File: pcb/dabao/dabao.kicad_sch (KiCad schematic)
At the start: 68 parts, among them J1 Conn_01x05, J2 USB_C_Receptacle_USB2.0_16P, J3 Conn_01x04, J4 MagConn_01x04_Pin, J5 Conn_Battery, J6 Conn_01x04, J7 Conn_01x04, J8 Display, SW1 SW_RESET, SW2 SW_POWER, U1 nice_nano, U2 MCP23017_SP

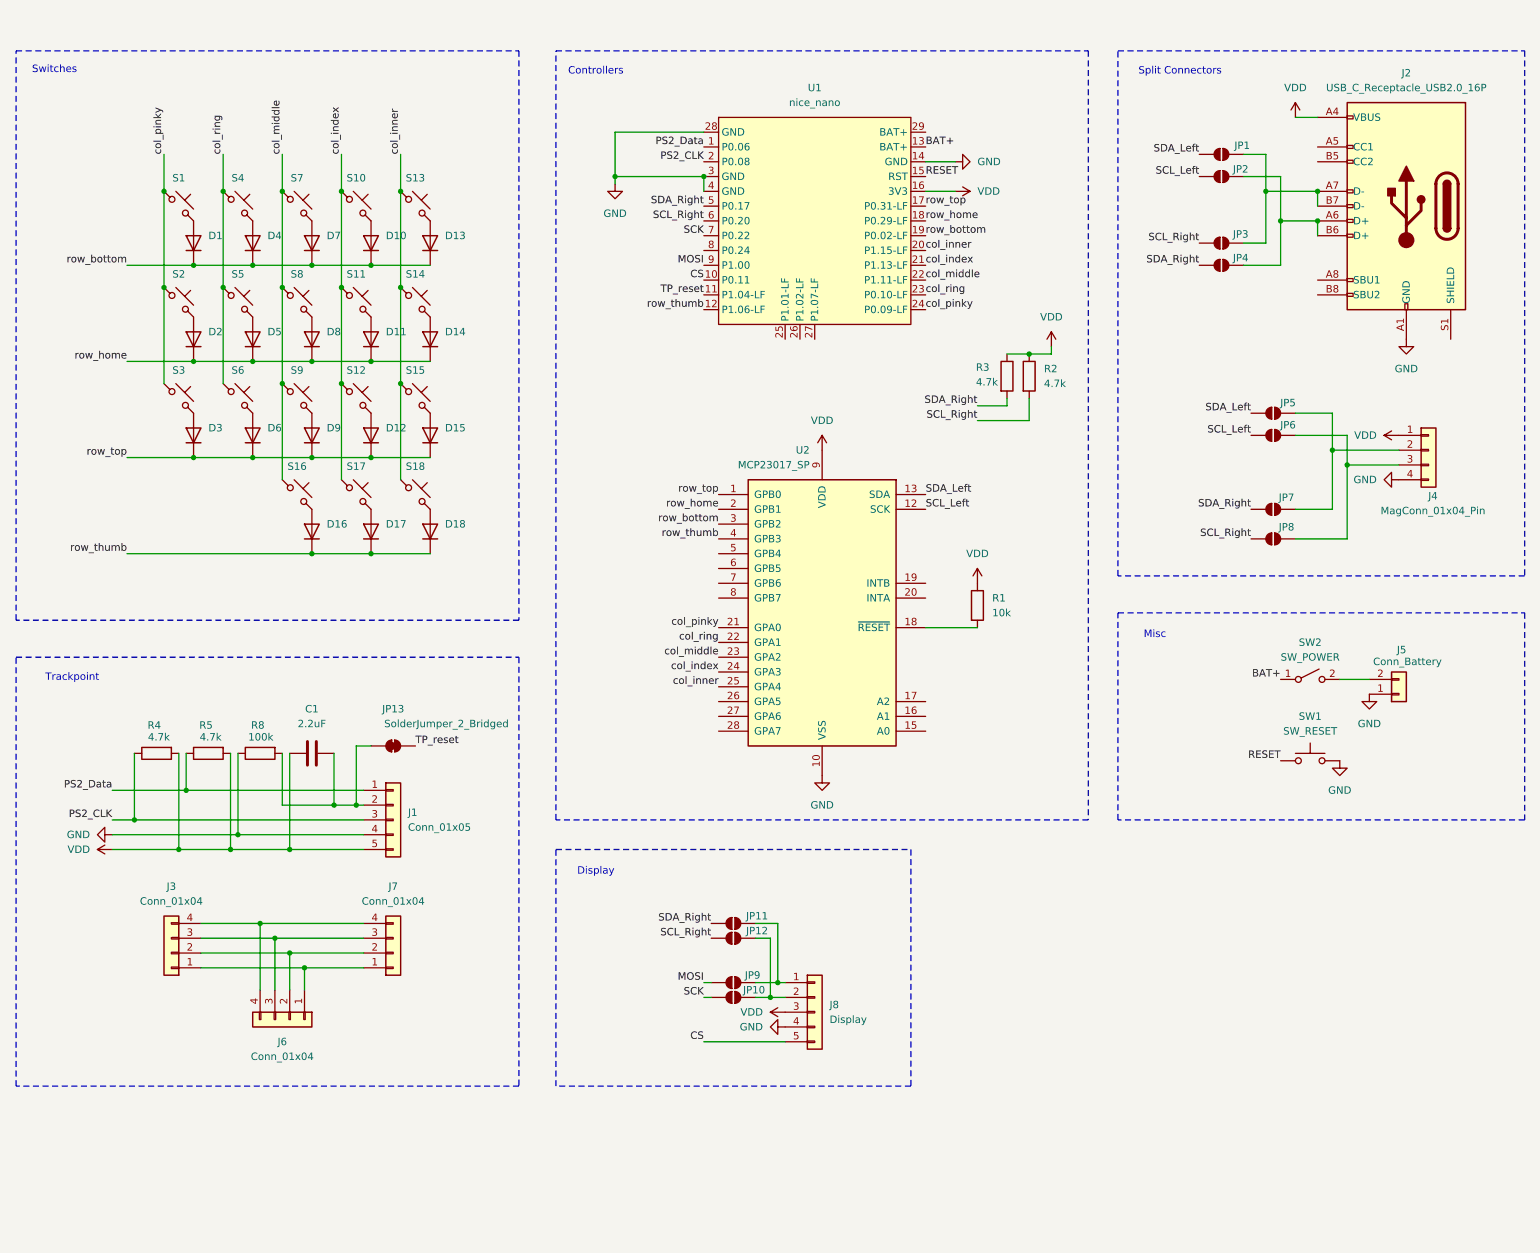
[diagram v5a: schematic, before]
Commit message: Move trackpoint to thumb, routing
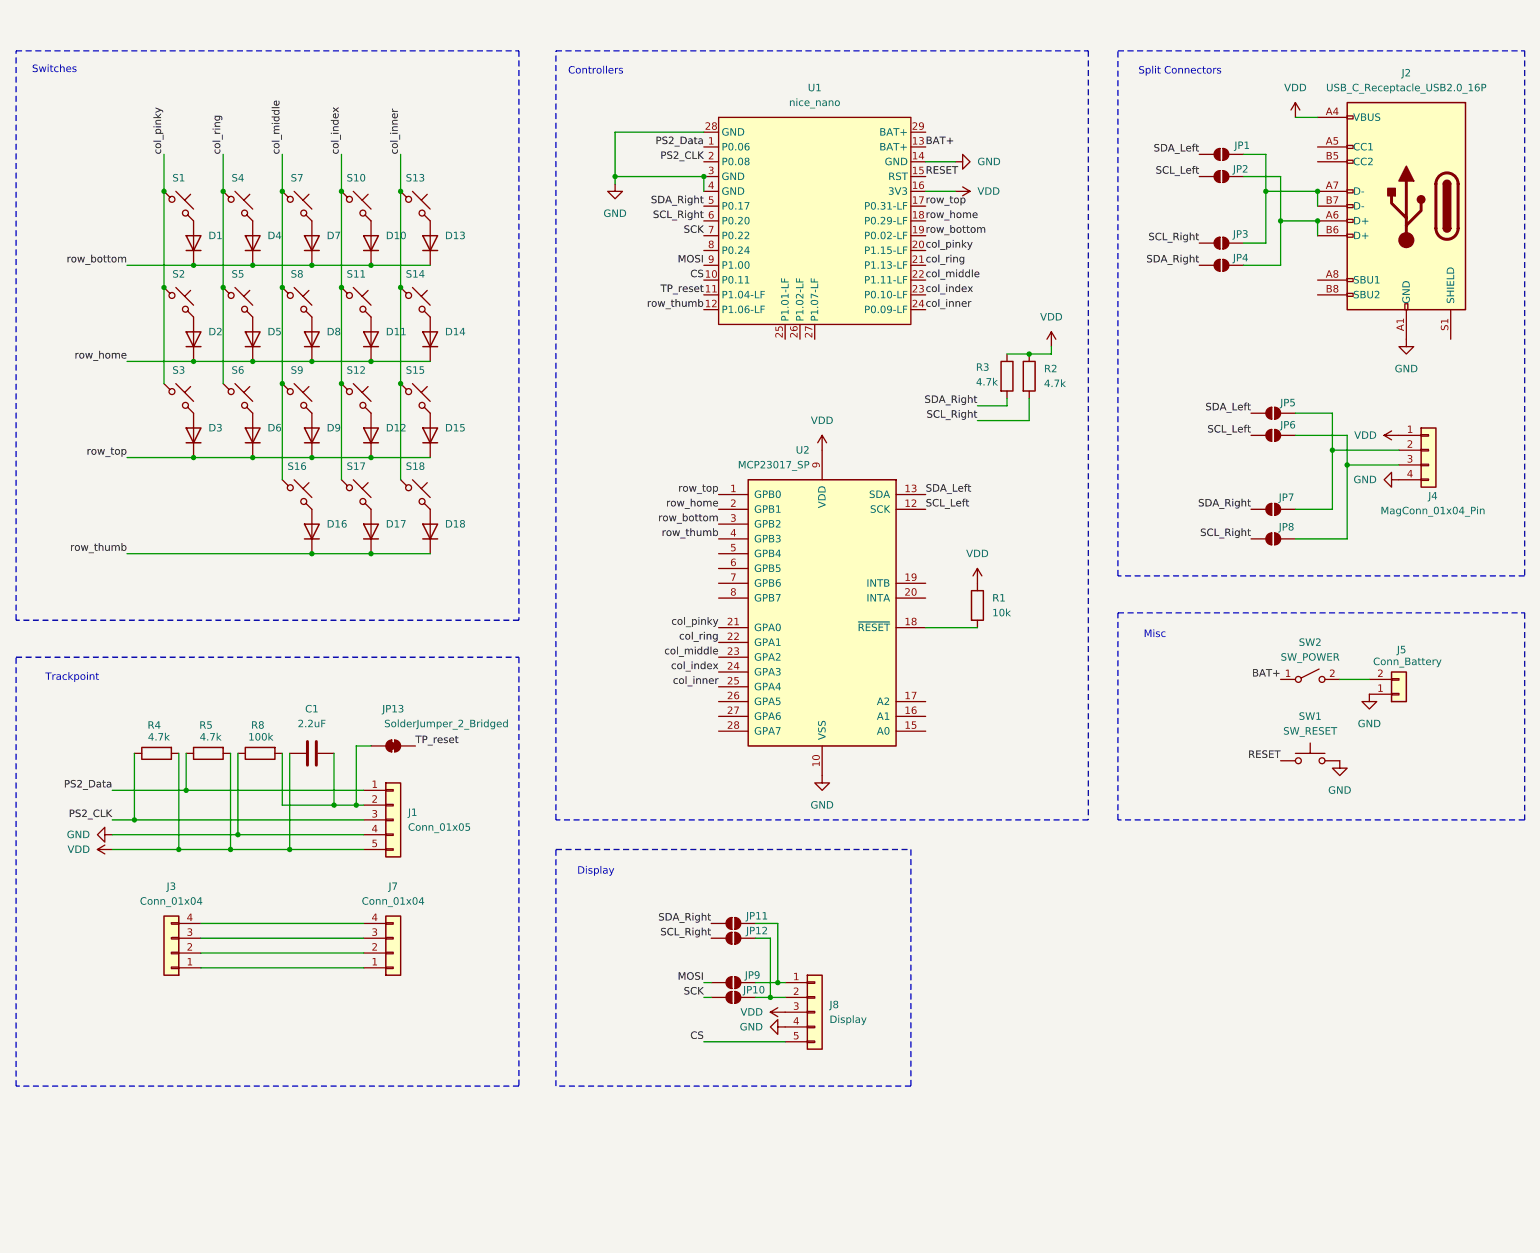
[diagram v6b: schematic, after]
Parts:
- removed J6: Conn_01x04, Library:TPSensorModule_Connector, symbol Connector_Generic:Conn_01x04
- S14, S16: footprint Library:SW_PG1350_reversible -> Library:Kailh_socket_PG1350_optional_reversible.kicad_mod
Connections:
- net col_index: now also U1.23 (P0.10-LF); no longer U1.21 (P1.13-LF)
- net col_inner: now also U1.24 (P0.09-LF); no longer U1.20 (P1.15-LF)
- net col_pinky: now also U1.20 (P1.15-LF); no longer U1.24 (P0.09-LF)
- net col_ring: now also U1.21 (P1.13-LF); no longer U1.23 (P0.10-LF)
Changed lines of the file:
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@@
 	)
 	(junction
-		(at 68.58 172.72)
-		(diameter 0)
-		(color 0 0 0 0)
-	)
-	(junction
 		(at 73.66 144.78)
 		(diameter 0)
@@
 	)
 	(junction
-		(at 63.5 167.64)
-		(diameter 0)
-		(color 0 0 0 0)
-	)
-	(junction
-		(at 66.04 170.18)
-		(diameter 0)
-		(color 0 0 0 0)
-	)
-	(junction
 		(at 242.57 39.37)
 		(diameter 0)
@@
 	)
 	(junction
-		(at 60.96 165.1)
-		(diameter 0)
-		(color 0 0 0 0)
-	)
-	(junction
 		(at 44.45 55.88)
 		(diameter 0)
@@
 	(wire
 		(pts
-			(xy 68.58 172.72) (xy 78.74 172.72)
+			(xy 50.8 172.72) (xy 78.74 172.72)
 		)
 		(stroke
@@
 	(wire
 		(pts
-			(xy 50.8 165.1) (xy 60.96 165.1)
+			(xy 50.8 165.1) (xy 78.74 165.1)
 		)
 		(stroke
@@
 	(wire
 		(pts
-			(xy 68.58 172.72) (xy 68.58 176.53)
-		)
-		(stroke
-			(width 0)
-			(type default)
-		)
-	)
-	(wire
-		(pts
 			(xy 80.01 52.07) (xy 90.17 52.07)
 		)
@@
 	(wire
 		(pts
-			(xy 50.8 170.18) (xy 66.04 170.18)
-		)
-		(stroke
-			(width 0)
-			(type default)
-		)
-	)
-	(wire
-		(pts
 			(xy 242.57 44.45) (xy 242.57 46.99)
 		)
@@
 	(wire
 		(pts
-			(xy 50.8 167.64) (xy 63.5 167.64)
-		)
-		(stroke
-			(width 0)
-			(type default)
-		)
-	)
-	(wire
-		(pts
 			(xy 245.11 83.82) (xy 256.54 83.82)
 		)
@@
 	(wire
 		(pts
-			(xy 50.8 172.72) (xy 68.58 172.72)
-		)
-		(stroke
-			(width 0)
-			(type default)
-		)
-	)
-	(wire
-		(pts
 			(xy 64.77 55.88) (xy 64.77 72.39)
 		)
@@
 	(wire
 		(pts
-			(xy 63.5 167.64) (xy 78.74 167.64)
+			(xy 50.8 167.64) (xy 78.74 167.64)
 		)
 		(stroke
@@
 	(wire
 		(pts
-			(xy 66.04 170.18) (xy 78.74 170.18)
+			(xy 50.8 170.18) (xy 78.74 170.18)
 		)
 		(stroke
@@
 	(wire
 		(pts
-			(xy 66.04 170.18) (xy 66.04 176.53)
-		)
-		(stroke
-			(width 0)
-			(type default)
-		)
-	)
-	(wire
-		(pts
 			(xy 38.1 52.07) (xy 49.53 52.07)
 		)
@@
 	(wire
 		(pts
-			(xy 60.96 165.1) (xy 60.96 176.53)
-		)
-		(stroke
-			(width 0)
-			(type default)
-		)
-	)
-	(wire
-		(pts
 			(xy 229.87 52.07) (xy 236.22 52.07)
 		)
@@
 	(wire
 		(pts
-			(xy 60.96 165.1) (xy 78.74 165.1)
-		)
-		(stroke
-			(width 0)
-			(type default)
-		)
-	)
-	(wire
-		(pts
 			(xy 44.45 39.37) (xy 44.45 55.88)
 		)
@@
 	(wire
 		(pts
-			(xy 63.5 167.64) (xy 63.5 176.53)
-		)
-		(stroke
-			(width 0)
-			(type default)
-		)
-	)
-	(wire
-		(pts
 			(xy 184.15 76.2) (xy 189.23 76.2)
 		)
@@
 		)
 	)
+	(label "col_inner"
+		(at 175.26 59.69 0)
+		(effects
+			(font
+				(size 1.27 1.27)
+			)
+			(justify left bottom)
+		)
+	)
 	(label "col_pinky"
 		(at 139.7 114.3 180)
@@
 		)
 	)
+	(label "col_ring"
+		(at 175.26 52.07 0)
+		(effects
+			(font
+				(size 1.27 1.27)
+			)
+			(justify left bottom)
+		)
+	)
 	(label "SDA_Right"
 		(at 138.43 165.1 180)
@@
 		)
 	)
-	(label "col_middle"
-		(at 175.26 54.61 0)
-		(effects
-			(font
-				(size 1.27 1.27)
-			)
-			(justify left bottom)
-		)
-	)
 	(label "BAT+"
 		(at 236.22 123.19 180)
@@
 		)
 	)
+	(label "col_index"
+		(at 175.26 57.15 0)
+		(effects
+			(font
+				(size 1.27 1.27)
+			)
+			(justify left bottom)
+		)
+	)
 	(label "SCL_Right"
 		(at 138.43 167.64 180)
@@
 		)
 	)
+	(label "col_middle"
+		(at 175.26 54.61 0)
+		(effects
+			(font
+				(size 1.27 1.27)
+			)
+			(justify left bottom)
+		)
+	)
 	(label "CS"
 		(at 137.16 54.61 180)
@@
 		)
 	)
+	(label "col_pinky"
+		(at 175.26 49.53 0)
+		(effects
+			(font
+				(size 1.27 1.27)
+			)
+			(justify left bottom)
+		)
+	)
 	(label "row_top"
 		(at 175.26 41.91 0)
@@
 		)
 	)
-	(label "col_pinky"
-		(at 175.26 59.69 0)
-		(effects
-			(font
-				(size 1.27 1.27)
-			)
-			(justify left bottom)
-		)
-	)
 	(label "SDA_Right"
 		(at 184.15 76.2 180)
@@
 		)
 	)
-	(label "col_ring"
-		(at 175.26 57.15 0)
-		(effects
-			(font
-				(size 1.27 1.27)
-			)
-			(justify left bottom)
-		)
-	)
 	(label "PS2_Data"
 		(at 35.56 142.24 180)
@@
 		)
 	)
-	(label "col_index"
-		(at 175.26 52.07 0)
-		(effects
-			(font
-				(size 1.27 1.27)
-			)
-			(justify left bottom)
-		)
-	)
 	(label "RESET"
 		(at 236.22 137.16 180)
@@
 		)
 	)
-	(label "col_inner"
-		(at 175.26 49.53 0)
-		(effects
-			(font
-				(size 1.27 1.27)
-			)
-			(justify left bottom)
-		)
-	)
 	(label "col_ring"
 		(at 54.61 33.02 90)
@@
 			)
 		)
-		(property "Footprint" "Library:SW_PG1350_reversible"
+		(property "Footprint" "Library:Kailh_socket_PG1350_optional_reversible.kicad_mod"
 			(at 67.31 91.44 0)
 			(effects
@@
 	)
 	(symbol
-		(lib_id "Connector_Generic:Conn_01x04")
-		(at 66.04 181.61 270)
-		(unit 1)
-		(exclude_from_sim no)
-		(in_bom yes)
-		(on_board yes)
-		(dnp no)
-		(fields_autoplaced yes)
-		(property "Reference" "J6"
-			(at 64.77 185.42 90)
-			(effects
-				(font
-					(size 1.27 1.27)
-				)
-			)
-		)
-		(property "Value" "Conn_01x04"
-			(at 64.77 187.96 90)
-			(effects
-				(font
-					(size 1.27 1.27)
-				)
-			)
-		)
-		(property "Footprint" "Library:TPSensorModule_Connector"
-			(at 66.04 181.61 0)
-			(effects
-				(font
-					(size 1.27 1.27)
-				)
-				(hide yes)
-			)
-		)
-		(property "Datasheet" "~"
-			(at 66.04 181.61 0)
-			(effects
-				(font
-					(size 1.27 1.27)
-				)
-				(hide yes)
-			)
-		)
-		(property "Description" "Generic connector, single row, 01x04, script generated (kicad-library-utils/schlib/autogen/connector/)"
-			(at 66.04 181.61 0)
-			(effects
-				(font
-					(size 1.27 1.27)
-				)
-				(hide yes)
-			)
-		)
-		(pin "1"
-		)
-		(pin "2"
-		)
-		(pin "3"
-		)
-		(pin "4"
-		)
-		(instances
-			(project ""
-				(path "/f7dfc45c-83ad-43c7-9815-463af0b28fbd"
-					(reference "J6")
-					(unit 1)
-				)
-			)
-		)
-	)
-	(symbol
 		(lib_id "Connector_Generic:Conn_01x05")
 		(at 83.82 147.32 0)
@@
 			)
 		)
-		(property "Footprint" "Library:SW_PG1350_reversible"
+		(property "Footprint" "Library:Kailh_socket_PG1350_optional_reversible.kicad_mod"
 			(at 87.63 58.42 0)
 			(effects

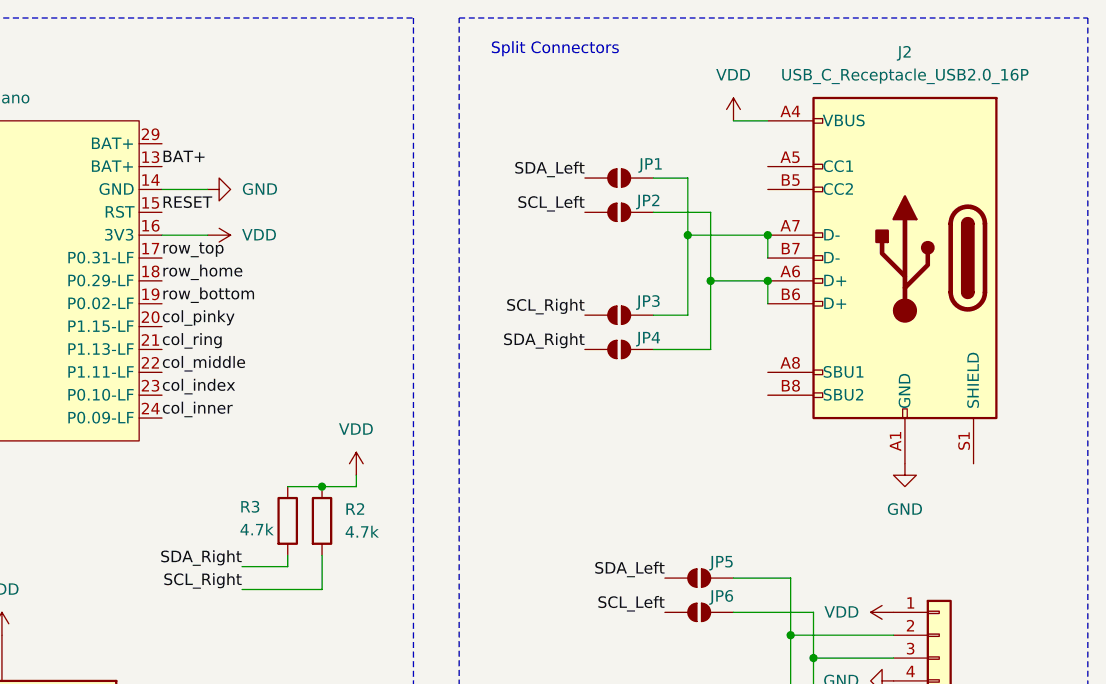
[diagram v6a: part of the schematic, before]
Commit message: Add nets, tweak layout
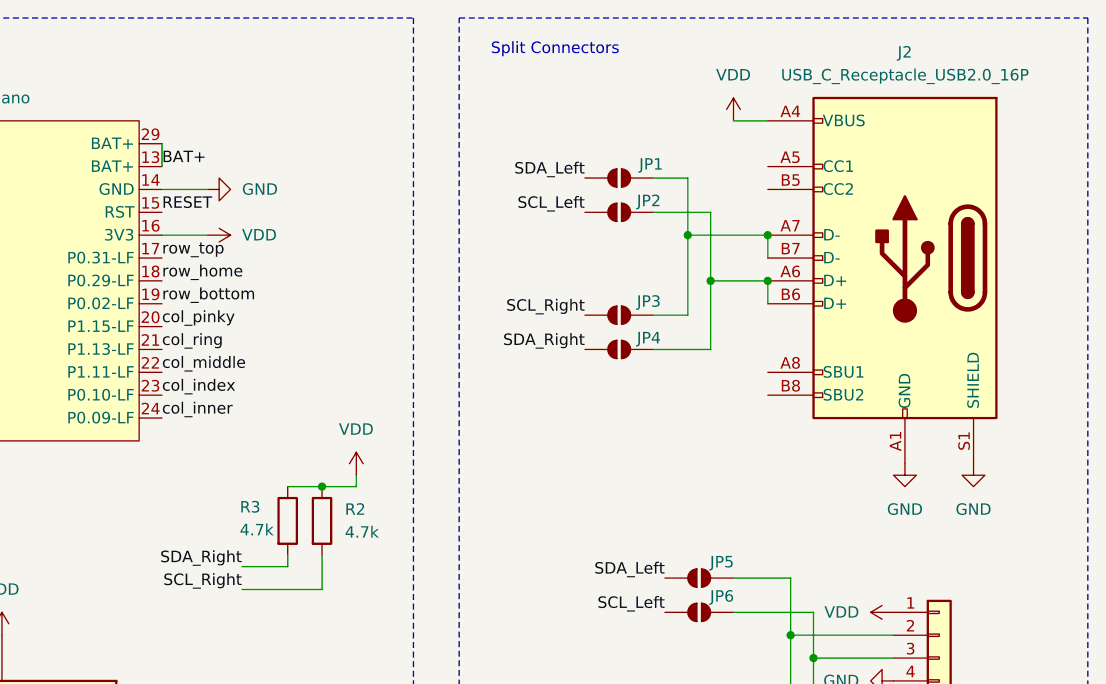
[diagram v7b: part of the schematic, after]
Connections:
- net BAT+: now also U1.29 (BAT+)
- net GND: now also J2.S1 (SHIELD)
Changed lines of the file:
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@@
 	(wire
 		(pts
+			(xy 175.26 29.21) (xy 175.26 31.75)
+		)
+		(stroke
+			(width 0)
+			(type default)
+		)
+	)
+	(wire
+		(pts
 			(xy 69.85 68.58) (xy 80.01 68.58)
 		)
@@
 					(unit 1)
 				)
+			)
+		)
+	)
+	(symbol
+		(lib_id "power:GND")
+		(at 265.43 64.77 0)
+		(unit 1)
+		(exclude_from_sim no)
+		(in_bom yes)
+		(on_board yes)
+		(dnp no)
+		(fields_autoplaced yes)
+		(property "Reference" "#PWR02"
+			(at 265.43 71.12 0)
+			(effects
+				(font
+					(size 1.27 1.27)
+				)
+				(hide yes)
+			)
+		)
+		(property "Value" "GND"
+			(at 265.43 69.85 0)
+			(effects
+				(font
+					(size 1.27 1.27)
+				)
+			)
+		)
+		(property "Footprint" ""
+			(at 265.43 64.77 0)
+			(effects
+				(font
+					(size 1.27 1.27)
+				)
+				(hide yes)
+			)
+		)
+		(property "Datasheet" ""
+			(at 265.43 64.77 0)
+			(effects
+				(font
+					(size 1.27 1.27)
+				)
+				(hide yes)
+			)
+		)
+		(property "Description" "Power symbol creates a global label with name \"GND\" , ground"
+			(at 265.43 64.77 0)
+			(effects
+				(font
+					(size 1.27 1.27)
+				)
+				(hide yes)
+			)
+		)
+		(pin "1"
+		)
+		(instances
+			(project "dabao"
+				(path "/f7dfc45c-83ad-43c7-9815-463af0b28fbd"
+					(reference "#PWR02")
+					(unit 1)
+				)
